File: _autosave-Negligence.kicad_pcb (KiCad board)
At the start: 2 copper layers, 228.9 x 105.7 mm, 116 parts, among them J1 AVR-ISP-6, SW1 keyboard_parts_KEYSW, SW10 keyboard_parts_KEYSW, SW11 keyboard_parts_KEYSW, SW12 keyboard_parts_KEYSW, SW13 keyboard_parts_KEYSW, SW14 keyboard_parts_KEYSW, SW15 keyboard_parts_KEYSW, SW16 keyboard_parts_KEYSW, SW17 keyboard_parts_KEYSW, SW18 keyboard_parts_KEYSW, SW19 keyboard_parts_KEYSW, SW2 keyboard_parts_KEYSW, SW20 keyboard_parts_KEYSW, SW21 keyboard_parts_KEYSW, SW22 keyboard_parts_KEYSW, SW23 keyboard_parts_KEYSW, SW24 keyboard_parts_KEYSW, SW25 keyboard_parts_KEYSW, SW26 keyboard_parts_KEYSW, SW27 keyboard_parts_KEYSW, SW28 keyboard_parts_KEYSW, SW29 keyboard_parts_KEYSW, SW3 keyboard_parts_KEYSW, SW30 keyboard_parts_KEYSW, SW31 keyboard_parts_KEYSW, SW32 keyboard_parts_KEYSW, SW33 keyboard_parts_KEYSW, SW34 keyboard_parts_KEYSW, SW35 keyboard_parts_KEYSW, SW36 keyboard_parts_KEYSW, SW37 keyboard_parts_KEYSW, SW38 keyboard_parts_KEYSW, SW39 keyboard_parts_KEYSW, SW4 keyboard_parts_KEYSW, SW40 keyboard_parts_KEYSW, SW41 keyboard_parts_KEYSW, SW42 keyboard_parts_KEYSW, SW43 keyboard_parts_KEYSW, SW44 keyboard_parts_KEYSW, SW45 keyboard_parts_KEYSW, SW46 keyboard_parts_KEYSW, SW47 RESET, SW48 BOOT, SW5 keyboard_parts_KEYSW, SW6 keyboard_parts_KEYSW, SW7 keyboard_parts_KEYSW, SW8 keyboard_parts_KEYSW, SW9 keyboard_parts_KEYSW, U1 ATmega328P-PU, Y1 16MHz

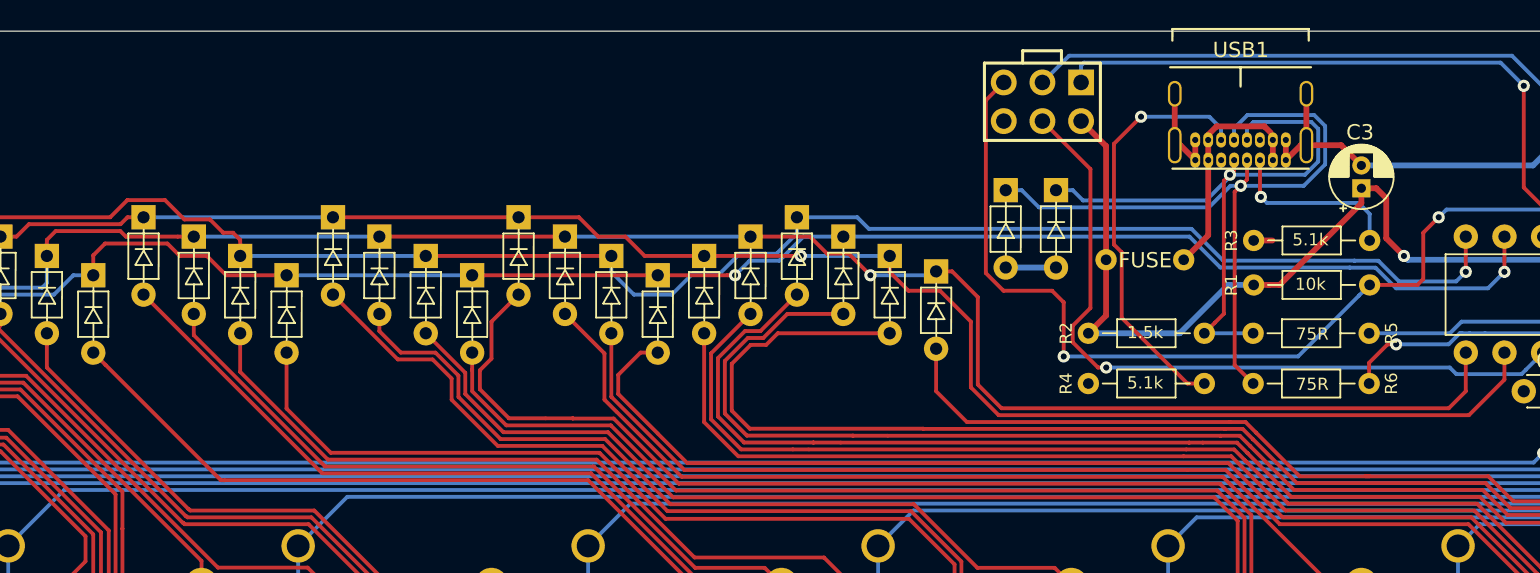
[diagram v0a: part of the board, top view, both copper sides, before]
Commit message: More diode routing
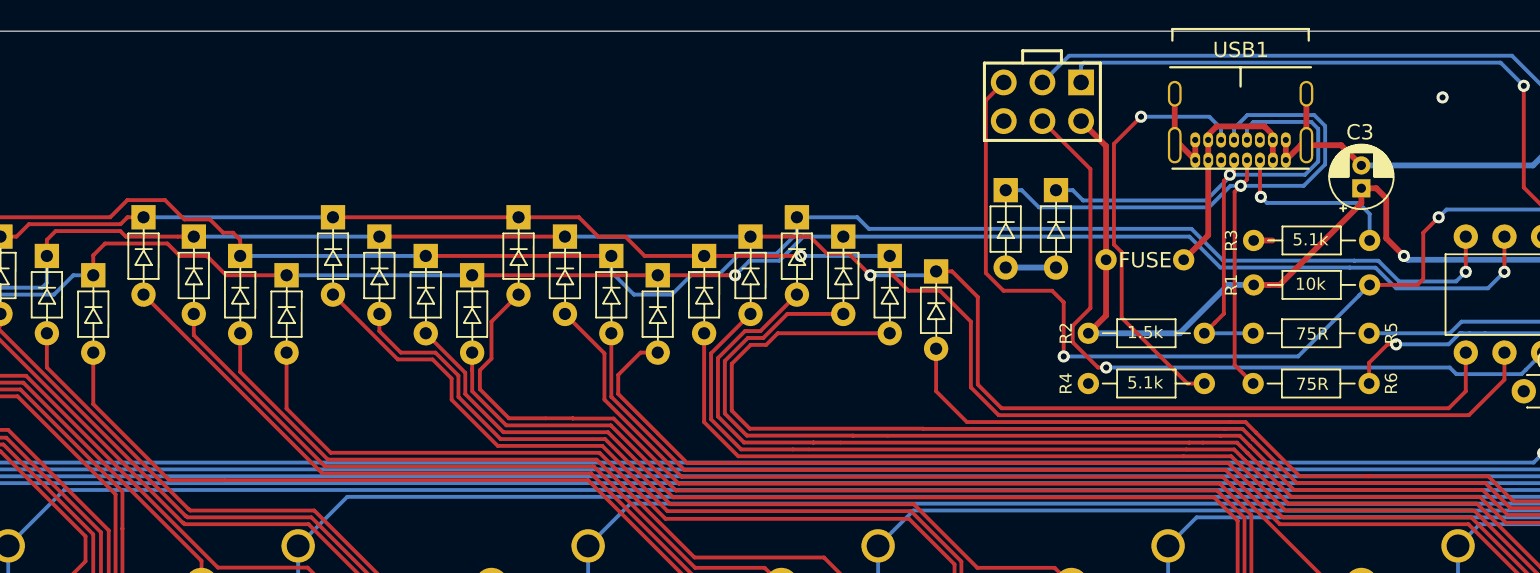
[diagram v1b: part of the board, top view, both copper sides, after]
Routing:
- net Net-(D32-Pad2): track 86.2 -> 88.2 mm
- net GND: vias 0 -> 1
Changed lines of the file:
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@@
     (thickness 1.6)
     (drawings 11)
-    (tracks 1041)
+    (tracks 1042)
     (zones 0)
     (modules 116)
@@
   (gr_arc (start 239.522 153.162) (end 239.522 155.702) (angle -90) (layer Edge.Cuts) (width 0.05))
   (gr_arc (start 15.748 153.162) (end 13.208 153.162) (angle -90) (layer Edge.Cuts) (width 0.05))
+  (via (at 195.834 54.356) (size 0.8) (drill 0.4) (layers F.Cu B.Cu) (net 1))
   (segment (start 221.60625 59.68125) (end 223.04375 61.11875) (width 0.381) (layer F.Cu) (net 1))
   (segment (start 221.60625 57.18175) (end 221.60625 59.68125) (width 0.381) (layer F.Cu) (net 1))
@@
   (segment (start 146.558 86.36) (end 139.7 79.502) (width 0.25) (layer F.Cu) (net 39))
   (segment (start 152.4 124.46) (end 146.558 118.618) (width 0.25) (layer F.Cu) (net 39))
-  (segment (start 107.987999 71.919999) (end 107.188 71.12) (width 0.254) (layer F.Cu) (net 39))
-  (segment (start 115.57 79.502) (end 107.987999 71.919999) (width 0.254) (layer F.Cu) (net 39))
-  (segment (start 115.824 79.502) (end 115.57 79.502) (width 0.254) (layer F.Cu) (net 39))
+  (segment (start 115.824 79.502) (end 112.182512 79.502) (width 0.254) (layer F.Cu) (net 39))
+  (segment (start 112.182512 79.502) (end 107.188 74.507488) (width 0.254) (layer F.Cu) (net 39))
+  (segment (start 107.188 74.507488) (end 107.188 71.12) (width 0.254) (layer F.Cu) (net 39))
   (segment (start 122.79119 77.70196) (end 119.888 74.79877) (width 0.25) (layer F.Cu) (net 40))
   (segment (start 140.4456 77.70196) (end 122.79119 77.70196) (width 0.25) (layer F.Cu) (net 40))
